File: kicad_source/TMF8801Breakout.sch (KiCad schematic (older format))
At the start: 25 parts, among them CN1 CONN_01X06, CN2 CONN_01X07, Q1 BSS138, Q2 BSS138, Q3 BSS138, U1 TPS736XX, U2 TMF8801

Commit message: added layout
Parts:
- added MECH1, MECH2: MHNP_2.1_4.0, MECH_mounting_holes:MH_210_400_NP, symbol MECH_mounting-holes:MHNP_2.1_4.0
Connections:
- wire segments 97 -> 99
- no-connect marks 1 -> 3
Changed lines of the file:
@@
 Text Label 8000 4950 0    50   ~ 0
 GPIO1
+$Comp
+L MECH_mounting-holes:MHNP_2.1_4.0 MECH1
+U 1 1 5FBF16DF
+P 6000 7100
+F 0 "MECH1" H 6128 7146 50  0000 L CNN
+F 1 "MHNP_2.1_4.0" H 6128 7055 50  0000 L CNN
+F 2 "MECH_mounting_holes:MH_210_400_NP" H 5900 7150 50  0001 C CNN
+F 3 "" H 6000 7100 50  0001 C CNN
+	1    6000 7100
+	1    0    0    -1
+$EndComp
+$Comp
+L MECH_mounting-holes:MHNP_2.1_4.0 MECH2
+U 1 1 5FBF1D85
+P 6000 7350
+F 0 "MECH2" H 6128 7396 50  0000 L CNN
+F 1 "MHNP_2.1_4.0" H 6128 7305 50  0000 L CNN
+F 2 "MECH_mounting_holes:MH_210_400_NP" H 5900 7400 50  0001 C CNN
+F 3 "" H 6000 7350 50  0001 C CNN
+	1    6000 7350
+	1    0    0    -1
+$EndComp
+NoConn ~ 5700 7100
+NoConn ~ 5700 7350
+Wire Wire Line
+	2750 3400 2750 3350
+Wire Wire Line
+	2750 2500 2750 2550
 $EndSCHEMATC

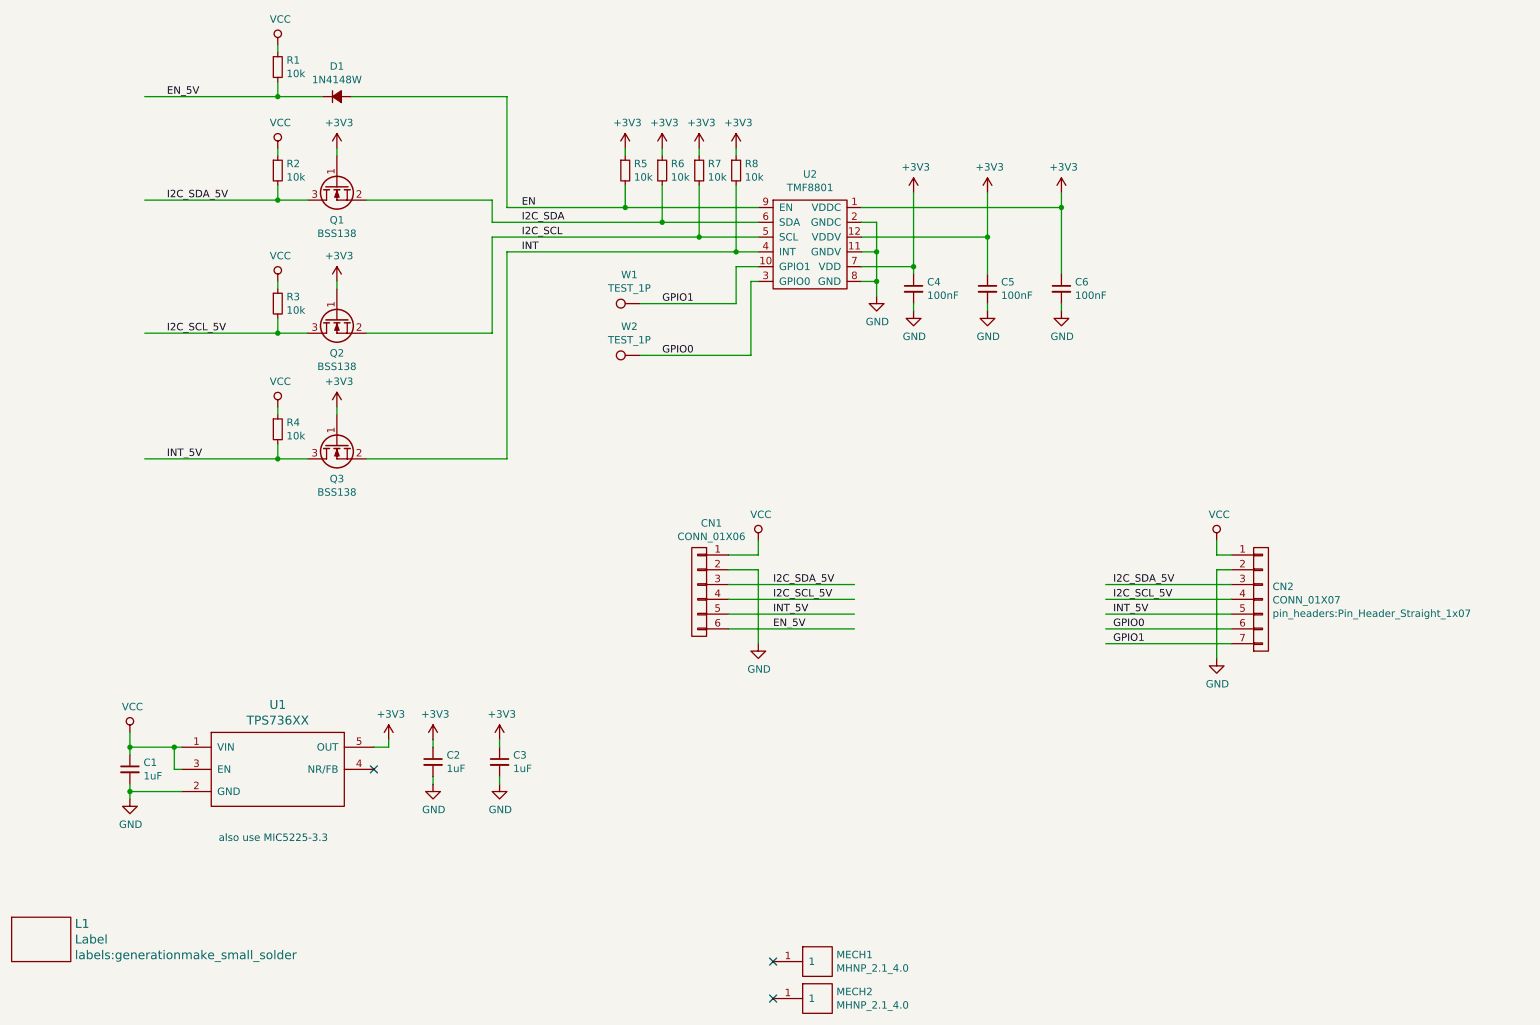
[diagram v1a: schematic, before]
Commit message: added Arduino ESLOV connector
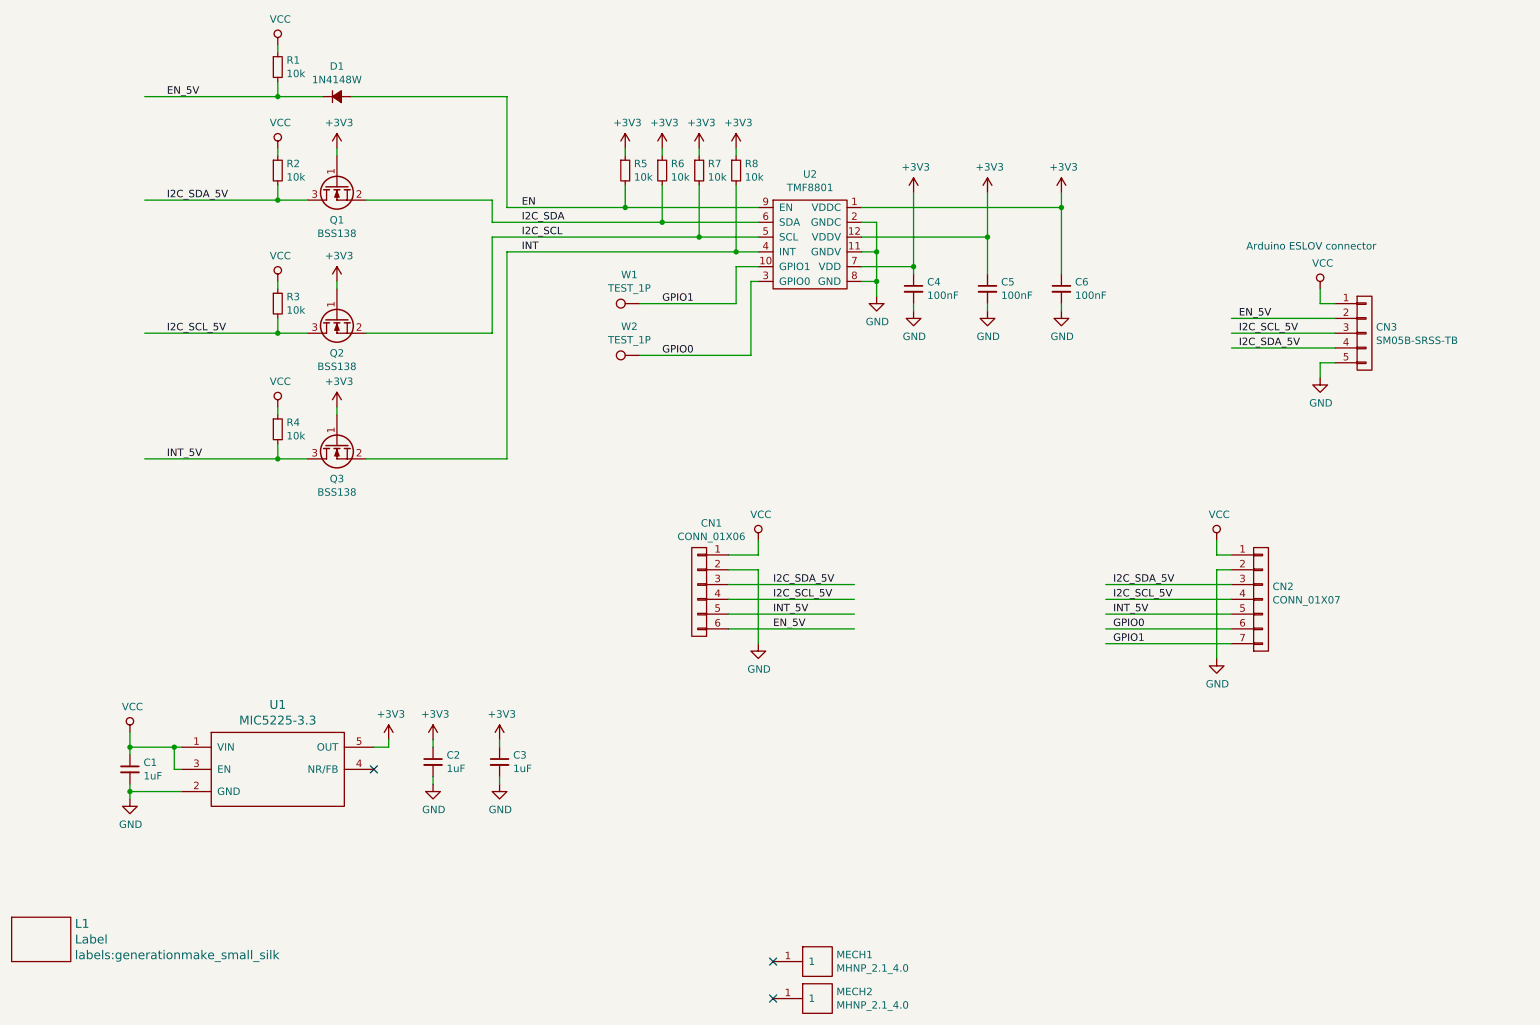
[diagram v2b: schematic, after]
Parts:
- added CN3: SM05B-SRSS-TB, Connector_JST:JST_SH_SM05B-SRSS-TB_1x05-1MP_P1.00mm_Horizontal, symbol mechanical-connectors:CONN_01X05
- L1: footprint labels:generationmake_small_solder -> labels:generationmake_small_silk
- U1: value TPS736XX -> MIC5225-3.3
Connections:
- wire segments 99 -> 106
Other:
- note added: "Arduino ESLOV connector"
- note removed: "also use MIC5225-3.3"
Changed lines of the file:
@@
 Sheet 1 1
 Title "TMF8801Breakout"
-Date "2020-11-24"
+Date "2020-11-25"
 Rev "0.1"
 Comp "genrationmake"
@@
 F 0 "L1" H 978 7056 60  0000 L CNN
 F 1 "Label" H 978 6950 60  0000 L CNN
-F 2 "labels:generationmake_small_solder" H 978 6844 60  0000 L CNN
+F 2 "labels:generationmake_small_silk" H 978 6844 60  0000 L CNN
 F 3 "" H 750 6950 60  0000 C CNN
 	1    750  6950
@@
 P 2350 5750
 F 0 "U1" H 2350 6137 60  0000 C CNN
-F 1 "TPS736XX" H 2350 6031 60  0000 C CNN
+F 1 "MIC5225-3.3" H 2350 6031 60  0000 C CNN
 F 2 "SOT_TO:SOT-23-5" H 2350 5900 60  0001 C CNN
 F 3 "" H 2350 5750 60  0000 C CNN
@@
 Wire Wire Line
 	5200 2200 5600 2200
-Text Notes 1950 6300 0    50   ~ 0
-also use MIC5225-3.3
 $Comp
 L devices:Q_NMOS_GSD Q1
@@
 F 0 "CN2" H 9078 4736 50  0000 L CNN
 F 1 "CONN_01X07" H 9078 4645 50  0000 L CNN
-F 2 "pin_headers:Pin_Header_Straight_1x07" H 9078 4554 50  0000 L CNN
+F 2 "pin_headers:Pin_Header_Straight_1x07" H 9078 4554 50  0001 L CNN
 F 3 "" H 9000 4650 50  0000 C CNN
 	1    9000 4650
@@
 Wire Wire Line
 	2750 2500 2750 2550
+$Comp
+L mechanical-connectors:CONN_01X05 CN3
+U 1 1 5FBEB318
+P 9700 2850
+F 0 "CN3" H 9778 2891 50  0000 L CNN
+F 1 "SM05B-SRSS-TB" H 9778 2800 50  0000 L CNN
+F 2 "Connector_JST:JST_SH_SM05B-SRSS-TB_1x05-1MP_P1.00mm_Horizontal" H 9700 2850 50  0001 C CNN
+F 3 "" H 9700 2850 50  0000 C CNN
+	1    9700 2850
+	1    0    0    -1
+$EndComp
+$Comp
+L power-supply:VCC #PWR030
+U 1 1 5FBED847
+P 9400 2550
+F 0 "#PWR030" H 9400 2400 50  0001 C CNN
+F 1 "VCC" H 9417 2723 50  0000 C CNN
+F 2 "" H 9400 2550 50  0000 C CNN
+F 3 "" H 9400 2550 50  0000 C CNN
+	1    9400 2550
+	1    0    0    -1
+$EndComp
+$Comp
+L power-supply:GND #PWR031
+U 1 1 5FBEF9B4
+P 9400 3150
+F 0 "#PWR031" H 9400 2900 50  0001 C CNN
+F 1 "GND" H 9405 2977 50  0000 C CNN
+F 2 "" H 9400 3150 50  0000 C CNN
+F 3 "" H 9400 3150 50  0000 C CNN
+	1    9400 3150
+	1    0    0    -1
+$EndComp
+Wire Wire Line
+	9500 3050 9400 3050
+Wire Wire Line
+	9400 3050 9400 3150
+Wire Wire Line
+	8800 2950 9500 2950
+Wire Wire Line
+	8800 2850 9500 2850
+Wire Wire Line
+	8800 2750 9500 2750
+Wire Wire Line
+	9400 2550 9400 2650
+Wire Wire Line
+	9400 2650 9500 2650
+Text Label 8850 2950 0    50   ~ 0
+I2C_SDA_5V
+Text Label 8850 2850 0    50   ~ 0
+I2C_SCL_5V
+Text Label 8850 2750 0    50   ~ 0
+EN_5V
+Text Notes 8900 2300 0    50   ~ 0
+Arduino ESLOV connector
 $EndSCHEMATC
